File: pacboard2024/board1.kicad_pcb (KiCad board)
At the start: 4 copper layers, 215 x 129.1 mm, 42 parts, among them J1 Conn_01x05_Female, J6 XT30 Male Connector, U1 BNO085, U2 ProS3

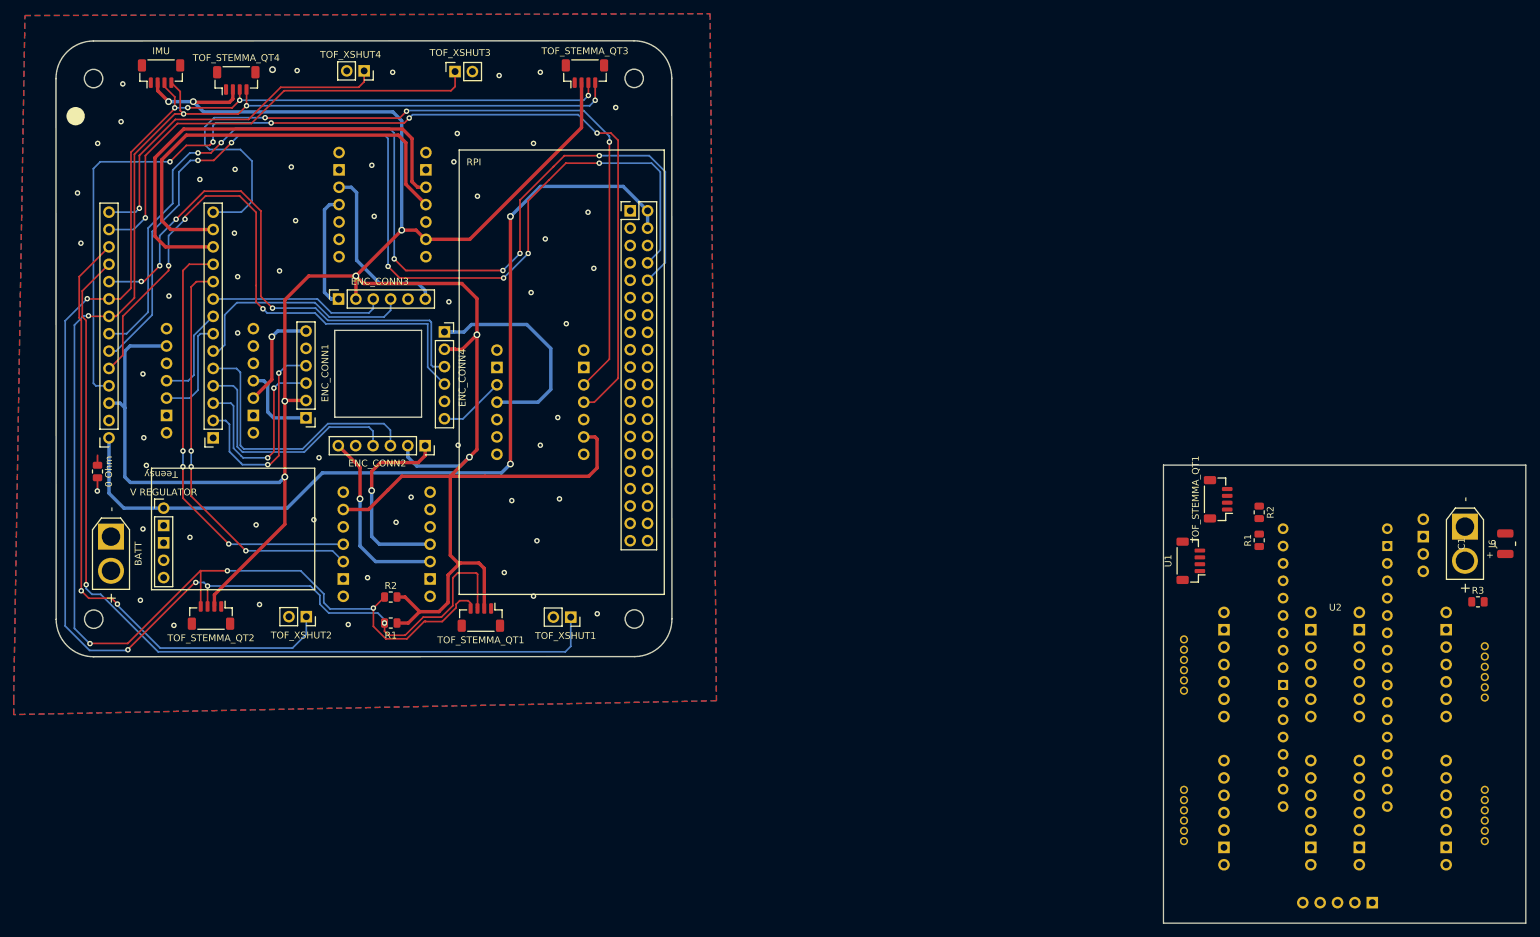
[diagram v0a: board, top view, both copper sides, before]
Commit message: schematic done(?) and layout
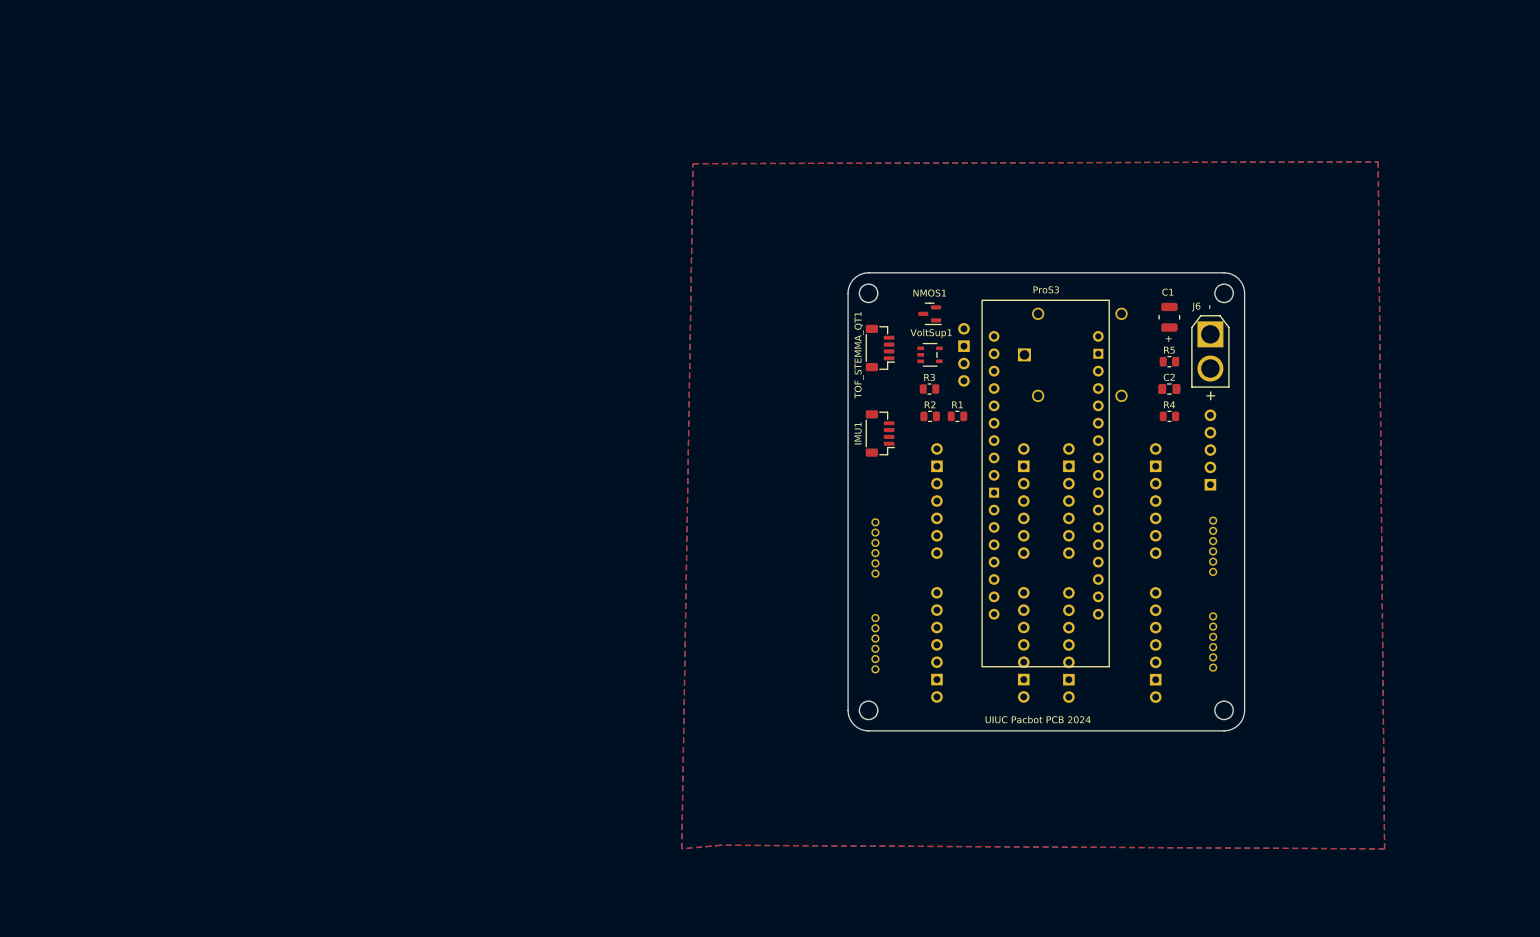
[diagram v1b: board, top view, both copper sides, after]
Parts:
- removed 0 Ohm: 0 Ohms, Resistor_SMD:R_0805_2012Metric
- removed BATT: XT30 Male Connector, Connector_AMASS:AMASS_XT30U-M_1x02_P5.0mm_Vertical
- removed the ENC_CONN1 at (54.6, 76.1)
- removed the ENC_CONN2 at (72.0, 80.2)
- removed the ENC_CONN3 at (59.3, 58.7)
- removed the ENC_CONN4 at (74.8, 63.5)
- removed IMU: BNO085, Connector_JST:JST_SH_BM04B-SRSS-TB_1x04-1MP_P1.00mm_Vertical
- removed the MC1 at (40.5, 84.1)
- removed the MC2 at (66.4, 108.1)
- removed the MC3 at (65.8, 31.4)
- removed the MC4 at (88.9, 60.3)
- removed the R1 at (67.0, 106.1)
- removed the R2 at (67.0, 102.3)
- removed RPI: Raspberry_PI_Zero_W, board1_footprints:Raspberry Pi Zero W
- removed the TOF_STEMMA_QT1 at (80.2, 105.3)
- removed TOF_STEMMA_QT2, TOF_STEMMA_QT3, TOF_STEMMA_QT4: Conn_01x04_Female, Connector_JST:JST_SH_BM04B-SRSS-TB_1x04-1MP_P1.00mm_Vertical
- removed TOF_XSHUT1, TOF_XSHUT2, TOF_XSHUT3, TOF_XSHUT4: Conn_01x02_Female, Connector_PinSocket_2.54mm:PinSocket_1x02_P2.54mm_Vertical
- removed Teensy: Teensy_4.0, board1_footprints:Teensy 4.0
- removed V REGULATOR: D24V50F5, board1_footprints:Voltage Regulator D24V50F5
- added C2: 0.1uF, Capacitor_SMD:C_0805_2012Metric_Pad1.18x1.45mm_HandSolder, F.Cu at (180.9, 71.9)
- added NMOS1: Q_NMOS_DGS, Package_TO_SOT_SMD:SOT-23, F.Cu at (145.8, 60.9)
- added R4: 1K Ohms, Resistor_SMD:R_0805_2012Metric, F.Cu at (180.9, 75.9)
- added R5: 100K Ohms, Resistor_SMD:R_0805_2012Metric, F.Cu at (180.9, 67.9)
- added Relay1: J107F1CS1224VDC.36, board1_footprints:J107, B.Cu at (159.7, 66.9)
- added VoltSup1: TPS3847085DBVR, board1_footprints:DBV5_TEX, F.Cu at (145.9, 66.9)
- C1: value C_Polarized -> 33uF
- moved R3 86.0 mm to (145.8, 71.9)
- moved VoltDiv1 72.7 mm to (150.8, 63.1)
- moved J1 65.6 mm to (186.9, 85.9), turned to 0 degrees
- moved ENC_CONN3 59.7 mm to (137.9, 98.9)
- moved C1 59.3 mm to (175.0, 61.4)
- moved ENC_CONN4 55.9 mm to (187.3, 91.1)
- moved TOF_STEMMA_QT1 54.2 mm to (138.5, 65.9)
- moved ProS3 50.8 mm to (162.9, 84.5)
- moved R2 50.1 mm to (145.9, 75.9), turned to 0 degrees
- moved IMU1 49.1 mm to (138.5, 78.4)
- moved MC1 49.1 mm to (172.5, 122.8)
- moved MC4 48.7 mm to (172.5, 74.8)
- moved MC2 48.6 mm to (153.2, 122.8)
- moved MC3 48.3 mm to (153.2, 74.8)
- moved R1 47.7 mm to (149.9, 75.9), turned to 0 degrees
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- renumbered U1 to IMU1, U2 to ProS3, U3 to VoltDiv1
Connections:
- C1 pad 2: /BATTERY_GROUND -> GNDREF
- J6 pad 1: /BATTERY_GROUND -> GNDREF
- J6 pad 2: /12V -> Net-(J6-Pin_2)
- MC1 pad 13: /BATTERY_GROUND -> GNDREF
- MC2 pad 13: /BATTERY_GROUND -> GNDREF
- MC3 pad 13: /BATTERY_GROUND -> GNDREF
- MC4 pad 13: /BATTERY_GROUND -> GNDREF
- R3 pad 1: GNDREF -> Net-(NMOS1-D)
- R3 pad 2: /BATTERY_GROUND -> Net-(Relay1-Coil_2)
- VoltDiv1 pad 3: /BATTERY_GROUND -> GNDREF
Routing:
- net /3V3_Teensy: track 384.1 -> 0.00 mm, vias 8 -> 0
- net /SDA_LINE: track 239.8 -> 0.00 mm, vias 9 -> 0
- net /SCL_LINE: track 237.7 -> 0.00 mm, vias 7 -> 0
- net /MC4_PWM2: track 158.1 -> 0.00 mm, vias 5 -> 0
- net /UART RXD (R PI): track 152.7 -> 0.00 mm, vias 6 -> 0
- net /UART TXD (R PI): track 149.4 -> 0.00 mm, vias 6 -> 0
- net /5V: track 132.5 -> 0.00 mm, vias 2 -> 0
- net /TOF_1_XSHUT: track 128.8 -> 0.00 mm, vias 1 -> 0
- net /MC4_PWM1: track 122.4 -> 0.00 mm, vias 3 -> 0
- net /TOF_2_XSHUT: track 92.2 -> 0.00 mm, vias 2 -> 0
- net /ENC_4_PINA: track 88.9 -> 0.00 mm, vias 3 -> 0
- net /ENC_4_PINB: track 78.8 -> 0.00 mm, vias 4 -> 0
- net /MC3_PWM1: track 69.3 -> 0.00 mm
- net /TOF_3_XSHUT: track 66.8 -> 0.00 mm, vias 1 -> 0
- net /MC3_PWM2: track 64.9 -> 0.00 mm
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- added copper zone on In1.Cu, net GNDREF
- removed copper zone on In1.Cu, net /BATTERY_GROUND
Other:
- board size 215 x 129.1 mm -> 58 x 67 mm
- board text added: "UIUC Pacbot PCB 2024"

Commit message: routing to pcb
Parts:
- moved VoltDiv1 17.4 mm to (168.0, 66.1), turned to 0 degrees
- moved R4 16.4 mm to (174.8, 60.7), turned to -90 degrees
- moved NMOS1 8.03 mm to (153.7, 62.5)
- moved R3 6.65 mm to (150.4, 67.1), turned to -90 degrees
- moved ProS3 6.41 mm to (162.8, 90.9)
- moved VoltSup1 5.04 mm to (148.3, 62.5)
- moved R2 4.83 mm to (150.7, 76.1), turned to 180 degrees
- moved Relay1 4.44 mm to (162.4, 63.4), turned to 90 degrees
- moved R1 3.07 mm to (146.8, 76.1), turned to 180 degrees
- moved R5 2.46 mm to (179.4, 65.9), turned to 180 degrees
- moved C1 1.62 mm to (173.4, 60.8)
- moved C2 1.04 mm to (181.1, 70.9)
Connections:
- ProS3 pad 10: /MC4_PWM1 -> /MC4_PWM2
- ProS3 pad 13: /MC4_PWM2 -> /MC1_PWM2
- ProS3 pad 14: /TOF_1_XSHUT -> /MC1_PWM1
- ProS3 pad 15: /TOF_2_XSHUT -> /ENC_4_PINB
- ProS3 pad 16: /TOF_3_XSHUT -> /ENC_4_PINA
- ProS3 pad 17: /TOF_4_XSHUT -> /ENC_1_PINA
- ProS3 pad 18: /ENC_2_PINB -> /ENC_1_PINB
- ProS3 pad 19: /ENC_3_PINA -> /ENC_2_PINB
- ProS3 pad 20: /ENC_3_PINB -> /ENC_2_PINA
- ProS3 pad 21: /ENC_4_PINA -> /MC2_PWM1
- ProS3 pad 22: /ENC_4_PINB -> /MC2_PWM2
- ProS3 pad 31: /MC1_PWM1 -> /ENC_3_PINB
- ProS3 pad 32: /ENC_1_PINA -> /ENC_3_PINA
- ProS3 pad 33: /ENC_1_PINB -> /MC3_PWM1
- ProS3 pad 34: /ENC_2_PINA -> /MC3_PWM2
- ProS3 pad 5: /MC1_PWM2 -> /TOF_1_XSHUT
- ProS3 pad 6: /MC2_PWM1 -> /TOF_2_XSHUT
- ProS3 pad 7: /MC2_PWM2 -> /TOF_3_XSHUT
- ProS3 pad 8: /MC3_PWM1 -> /TOF_4_XSHUT
- ProS3 pad 9: /MC3_PWM2 -> /MC4_PWM1
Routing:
- net GNDREF: track 0.00 -> 186.2 mm, vias 0 -> 34
- net /ENC_3_PINA: track 0.00 -> 95.2 mm
- net /ENC_3_PINB: track 0.00 -> 85.3 mm
- net /MOTOR_4_PIN1: track 0.00 -> 83.4 mm, vias 0 -> 1
- net /MOTOR_4_PIN2: track 0.00 -> 81.6 mm, vias 0 -> 1
- net /3V3: track 0.00 -> 76.6 mm, vias 0 -> 14
- net /ENC_1_PINB: track 0.00 -> 58.0 mm, vias 0 -> 2
- net Net-(J6-Pin_2): track 0.00 -> 56.0 mm
- net /MOTOR_2_PIN1: track 0.00 -> 42.8 mm, vias 0 -> 2
- net /MOTOR_2_PIN2: track 0.00 -> 42.4 mm, vias 0 -> 2
- net Net-(VoltSup1-*RESET): track 0.00 -> 37.2 mm
- net /ENC_1_PINA: track 0.00 -> 35.0 mm
- net /ENC_2_PINA: track 0.00 -> 34.6 mm
- net /SDA_LINE: track 0.00 -> 34.3 mm
- net /SCL_LINE: track 0.00 -> 33.4 mm, vias 0 -> 2
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- added copper zone on In1.Cu, net /12V
- added copper zone on In2.Cu, net /3V3
- removed copper zone on In2.Cu, net /12V
- removed copper zone on In1.Cu, net GNDREF
